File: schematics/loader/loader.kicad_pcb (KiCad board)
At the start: 2 copper layers, 102 x 96 mm, 16 parts, among them J1 Bus, J2 Bus, J4 to Microcode, SW1 RESET, U1 74HC595, U2 74LS00, U3 74HC595, U4 DM-OLED096-636

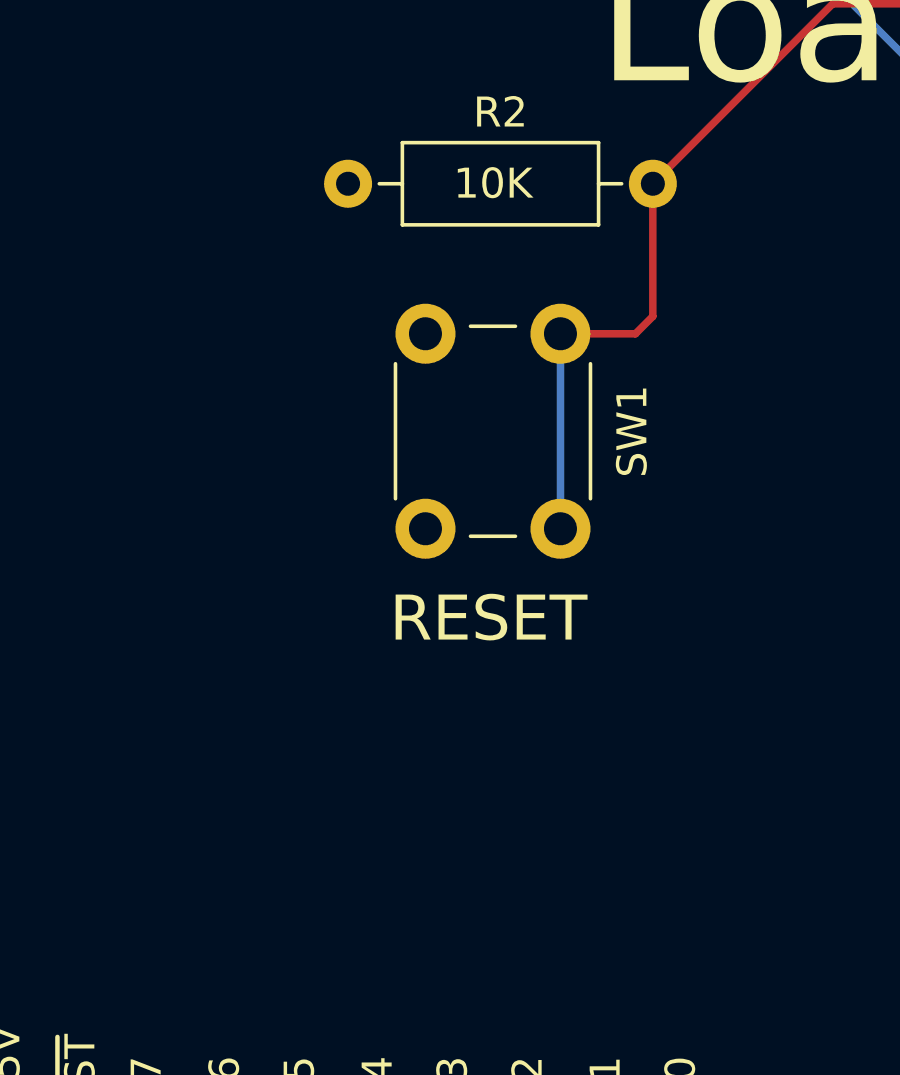
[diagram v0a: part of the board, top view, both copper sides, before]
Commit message: Change Loader reset button
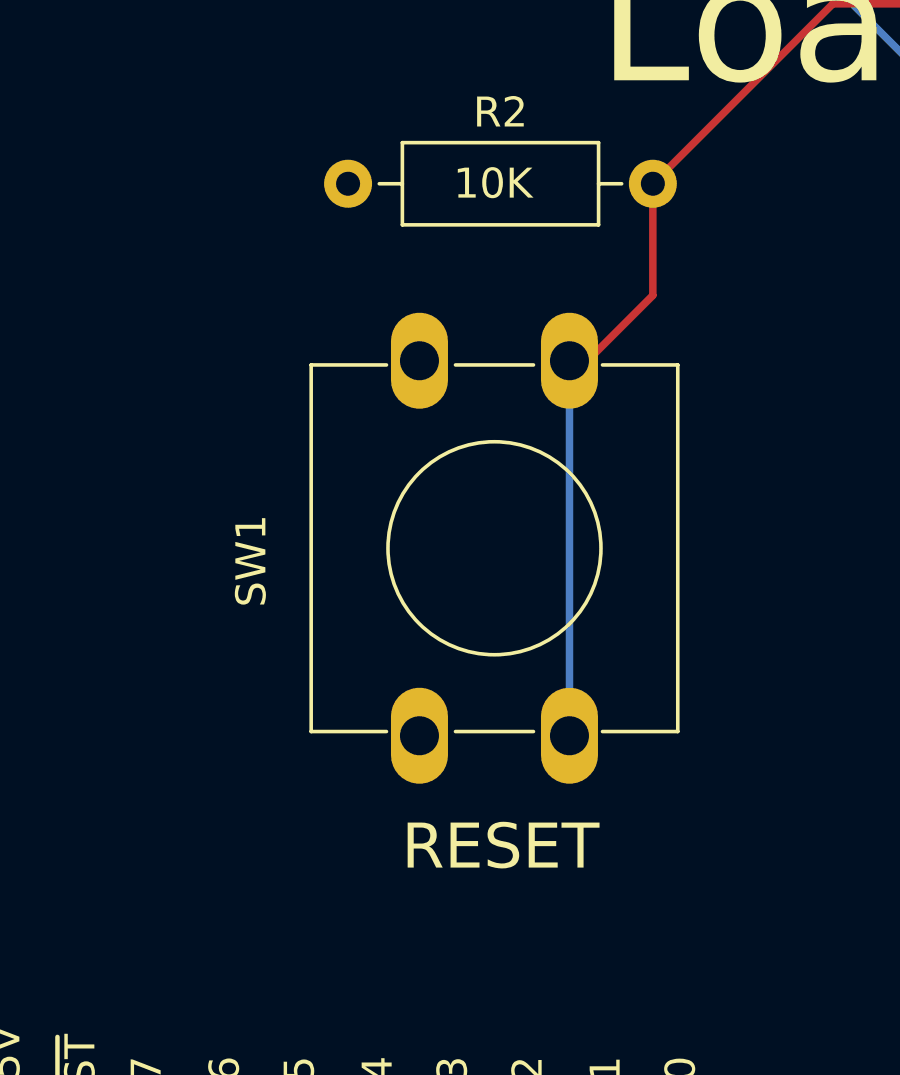
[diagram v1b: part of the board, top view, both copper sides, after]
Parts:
- SW1: footprint Button_Switch_THT:SW_PUSH_6mm -> Button_Switch_THT:SW_PUSH-12mm
- moved SW1 6.90 mm to (102.8, 121.4)
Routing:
- net /~{BT-R}: track 74.8 -> 80.4 mm

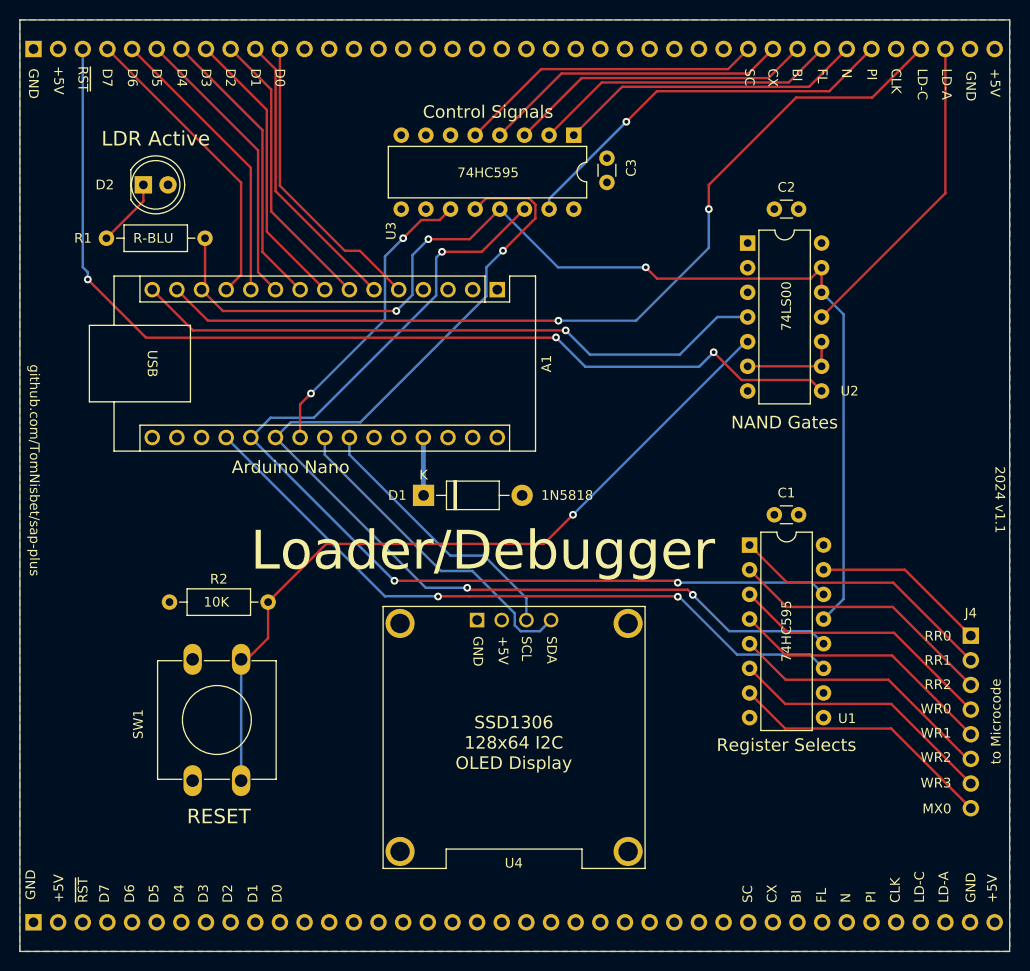
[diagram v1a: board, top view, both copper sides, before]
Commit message: Arduino Loader Module v1.2 schematics and code
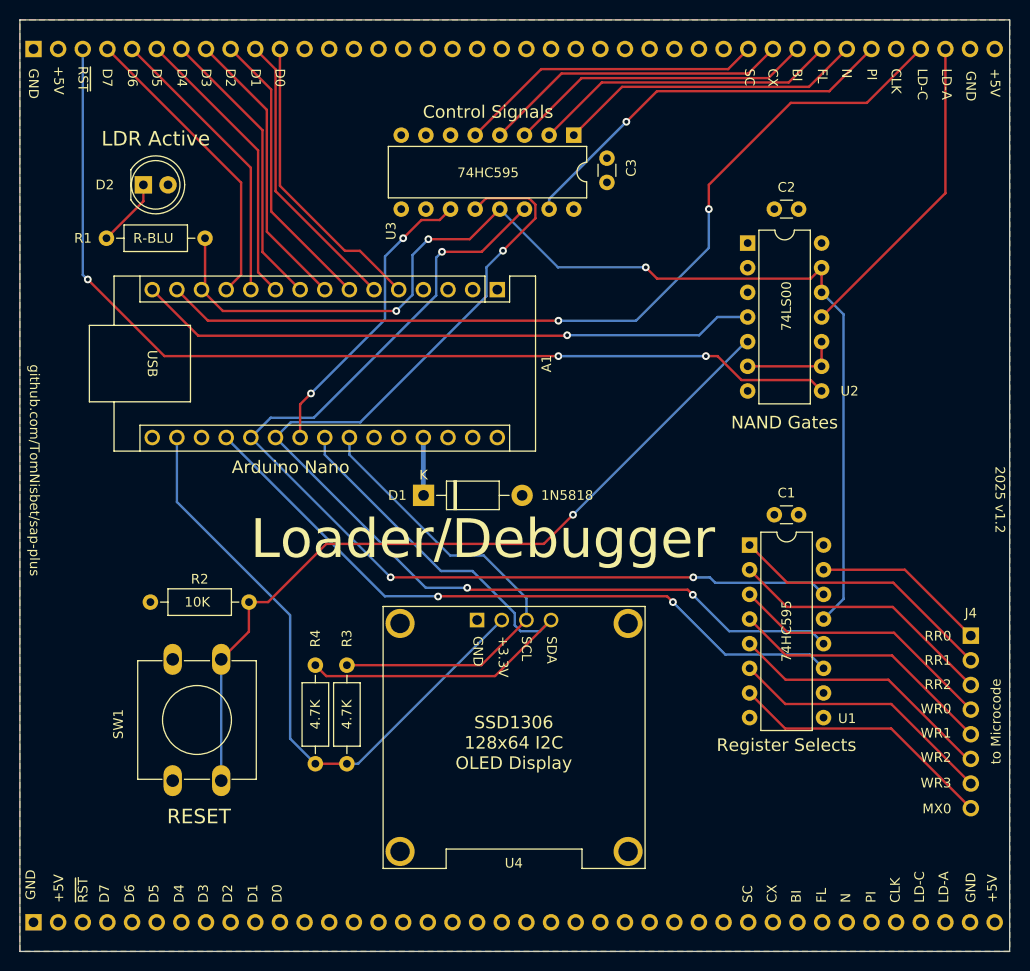
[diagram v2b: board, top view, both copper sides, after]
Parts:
- added R3: 4.7K, Resistor_THT:R_Axial_DIN0207_L6.3mm_D2.5mm_P10.16mm_Horizontal, F.Cu at (118.7, 119.7)
- added R4: 4.7K, Resistor_THT:R_Axial_DIN0207_L6.3mm_D2.5mm_P10.16mm_Horizontal, F.Cu at (115.5, 119.7)
- moved SW1 2.05 mm to (100.8, 121.4)
- moved R2 1.97 mm to (98.5, 103.0)
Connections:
- A1 pad 17: unconnected-(A1-3V3-Pad17) -> Net-(A1-3V3)
- U4 pad 2: +5V -> Net-(A1-3V3)
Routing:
- net Net-(A1-3V3): track 0.00 -> 64.9 mm
- net /SDA: track 33.8 -> 61.0 mm
- net /SCL: track 28.4 -> 48.8 mm
- net /~{BT-R}: track 80.4 -> 82.1 mm
- net /~{LD-R}: track 65.7 -> 64.1 mm
- net ~{RST}: track 105.6 -> 104.4 mm
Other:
- board text added: "+3.3V"
- board text added: "2025 v${REVISION}"
- board text removed: "2024 v${REVISION}"
